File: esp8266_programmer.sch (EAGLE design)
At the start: 24 parts, among them IC2 UA78M05DCY, J1 10118193-0001LF, Q1 12mhz, Q2 ON_SEMICONDUCTOR_BC849BLT1GON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, Q3 ON_SEMICONDUCTOR_BC849BLT1GON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

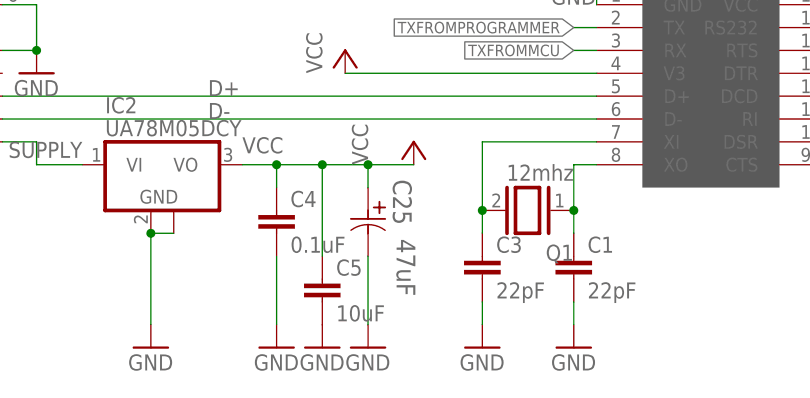
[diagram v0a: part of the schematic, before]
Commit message: Added library for USB port
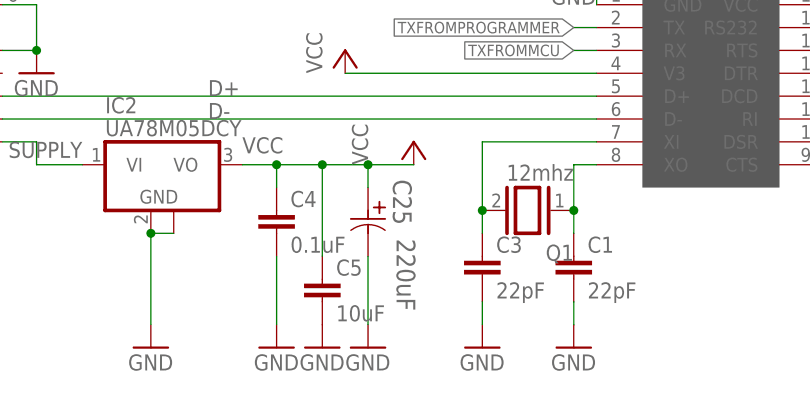
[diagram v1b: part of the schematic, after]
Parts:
- C25: value 47uF -> 220uF
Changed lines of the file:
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@@
 <part name="C4" library="rcl" library_urn="urn:adsk.eagle:library:334" deviceset="C-EU" device="C0603" package3d_urn="urn:adsk.eagle:package:23616/2" value="0.1uF"/>
 <part name="C5" library="rcl" library_urn="urn:adsk.eagle:library:334" deviceset="C-EU" device="C0603" package3d_urn="urn:adsk.eagle:package:23616/2" value="10uF"/>
-<part name="C25" library="Panasonic-EEEFK_EEEFP" deviceset="EEE-" device="-CASE-F" technology="FK1C471P" value="47uF"/>
+<part name="C25" library="Panasonic-EEEFK_EEEFP" deviceset="EEE-" device="-CASE-F" technology="FK1C471P" value="220uF"/>
 <part name="GND4" library="supply1" library_urn="urn:adsk.eagle:library:371" deviceset="GND" device=""/>
 <part name="GND5" library="supply1" library_urn="urn:adsk.eagle:library:371" deviceset="GND" device=""/>
